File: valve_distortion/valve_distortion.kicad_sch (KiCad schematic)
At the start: 30 parts, among them J1 INPUT, J2 OUTPUT, J3 Barrel_Jack, SW1 SW_DPDT_x2, U1 12AX7, U2 TL074

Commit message: Finish layout
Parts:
- removed D1: ENABLE, Connector_PinHeader_2.54mm:PinHeader_1x02_P2.54mm_Vertical, symbol Device:LED
- removed R5: 100k, Resistor_THT:R_Axial_DIN0207_L6.3mm_D2.5mm_P10.16mm_Horizontal, symbol Device:R
- added C5: 16pF, Capacitor_THT:C_Disc_D3.0mm_W1.6mm_P2.50mm, symbol Device:C_Small
- added D1: LED IND 12V, Connector_PinHeader_2.54mm:PinHeader_1x02_P2.54mm_Vertical, symbol Connector_Generic:Conn_01x02
- added D3: 1N5817, Diode_THT:D_DO-41_SOD81_P10.16mm_Horizontal, symbol Diode:1N5817
- added Q1: 2N3904, Package_TO_SOT_THT:TO-92_Inline, symbol Transistor_BJT:2N3904
- added R11, R13, R7, R8: 100k, Resistor_THT:R_Axial_DIN0207_L6.3mm_D2.5mm_P10.16mm_Horizontal, symbol Device:R
- added R2: 100R, Resistor_THT:R_Axial_DIN0207_L6.3mm_D2.5mm_P10.16mm_Horizontal, symbol Device:R
- D2: value SIGNAL -> NTE30033
- J1, J2: footprint Connector_Molex:Molex_KK-254_AE-6410-02A_1x02_P2.54mm_Vertical -> Connector_PinHeader_2.54mm:PinHeader_1x02_P2.54mm_Vertical
- R12: renamed from R7; value 1k -> 470R
- R6: value 1k -> 100k
- RV4: value R_Potentiometer_Trim -> 200k; footprint Potentiometer_THT:Potentiometer_Bourns_3266Y_Vertical -> valve_distortion:Trimmer
- renumbered C9 to C10, C5 to C6, C6 to C7, C7 to C8, C8 to C9, R9 to R10, R2 to R3, R3 to R5, R8 to R9
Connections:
- net +12V: now also SW1.4 (A), D3.1 (K); no longer J3.1, SW1.5 (B)
- net GND: now also SW1.6 (C), U1.3 (K), D1.2 (Pin_2), Q1.1 (E); no longer D2.1 (K), U1.8 (K)
- net VBIAS: now also U2.10 (+), U2.5 (+), R11.1, R7.2; no longer C8.1, U2.1, U2.12 (+), U2.2 (-)
- net at C3.1, R5.2: now also U1.1 (A); no longer U1.6 (A)
- net at C2.1, R4.1: now also U1.2 (G); no longer U1.7 (G)
- net at C2.2, R3.2: now also U1.6 (A); no longer U1.1 (A)
- net at C1.1, R1.1: now also U1.7 (G); no longer U1.2 (G)
- net at RV1.3: now also R2.2; no longer U1.3 (K)
- net at C3.2, C4.2: now also R6.2; no longer U2.10 (+), U2.5 (+)
- net at U2.6 (-): now also R6.1, C5.2, R7.1, R8.2; no longer RV4.2
- net at R12.1: now also U2.14; no longer U2.7
- net at U2.8, U2.9 (-): no longer C6.1
- net at U2.13 (-): now also RV4.2; no longer U2.14
- new net: R2.1, U1.8 (K)
- new net: C8.1, R11.2, U2.1, U2.2 (-)
- new net: Q1.2 (B), R13.1
- new net: D2.1 (K), Q1.3 (C)
- new net: D3.2 (A), J3.1
- new net BUF_OUT: C5.1, C6.1, R8.1, U2.12 (+), U2.7
- new net ENABLE: D1.1 (Pin_1), R13.2, SW1.5 (B)
- no-connect marks 2 -> 1
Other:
- note added: "ENABLE LED"
- note added: "Inverting Summer Gain = -1"
- note added: "SIGNAL LED"
- note removed: "GAIN"
- note removed: "RC High-pass Fc = ~3.4Hz"
- note removed: "RC High-pass Fc = ~7.2Hz"
- note removed: "TONE"
- note removed: "VOLUME"
- moved on the sheet: C1, C10, C2, C3, C6, C7, C8, C9, D2, J1, J2, J3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

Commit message: Include changes from scehmatic review
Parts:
- removed R11: 100k, Resistor_THT:R_Axial_DIN0207_L6.3mm_D2.5mm_P10.16mm_Horizontal, symbol Device:R
- added R12, R8: 100k, Resistor_THT:R_Axial_DIN0207_L6.3mm_D2.5mm_P10.16mm_Horizontal, symbol Device:R
- renumbered R9 to R10, R10 to R11, R12 to R13, R13 to R14, R7 to R6, R6 to R7, R8 to R9
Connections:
- net VBIAS: now also C8.1, U2.1, U2.2 (-), R12.2, R8.2; no longer U2.10 (+), U2.5 (+)
- new net: R8.1, U2.5 (+)
- new net: R12.1, U2.10 (+)
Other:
- moved on the sheet: C4, C5, C6, C7, C8, D1, J2, R10, R11, R6, R7, R9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

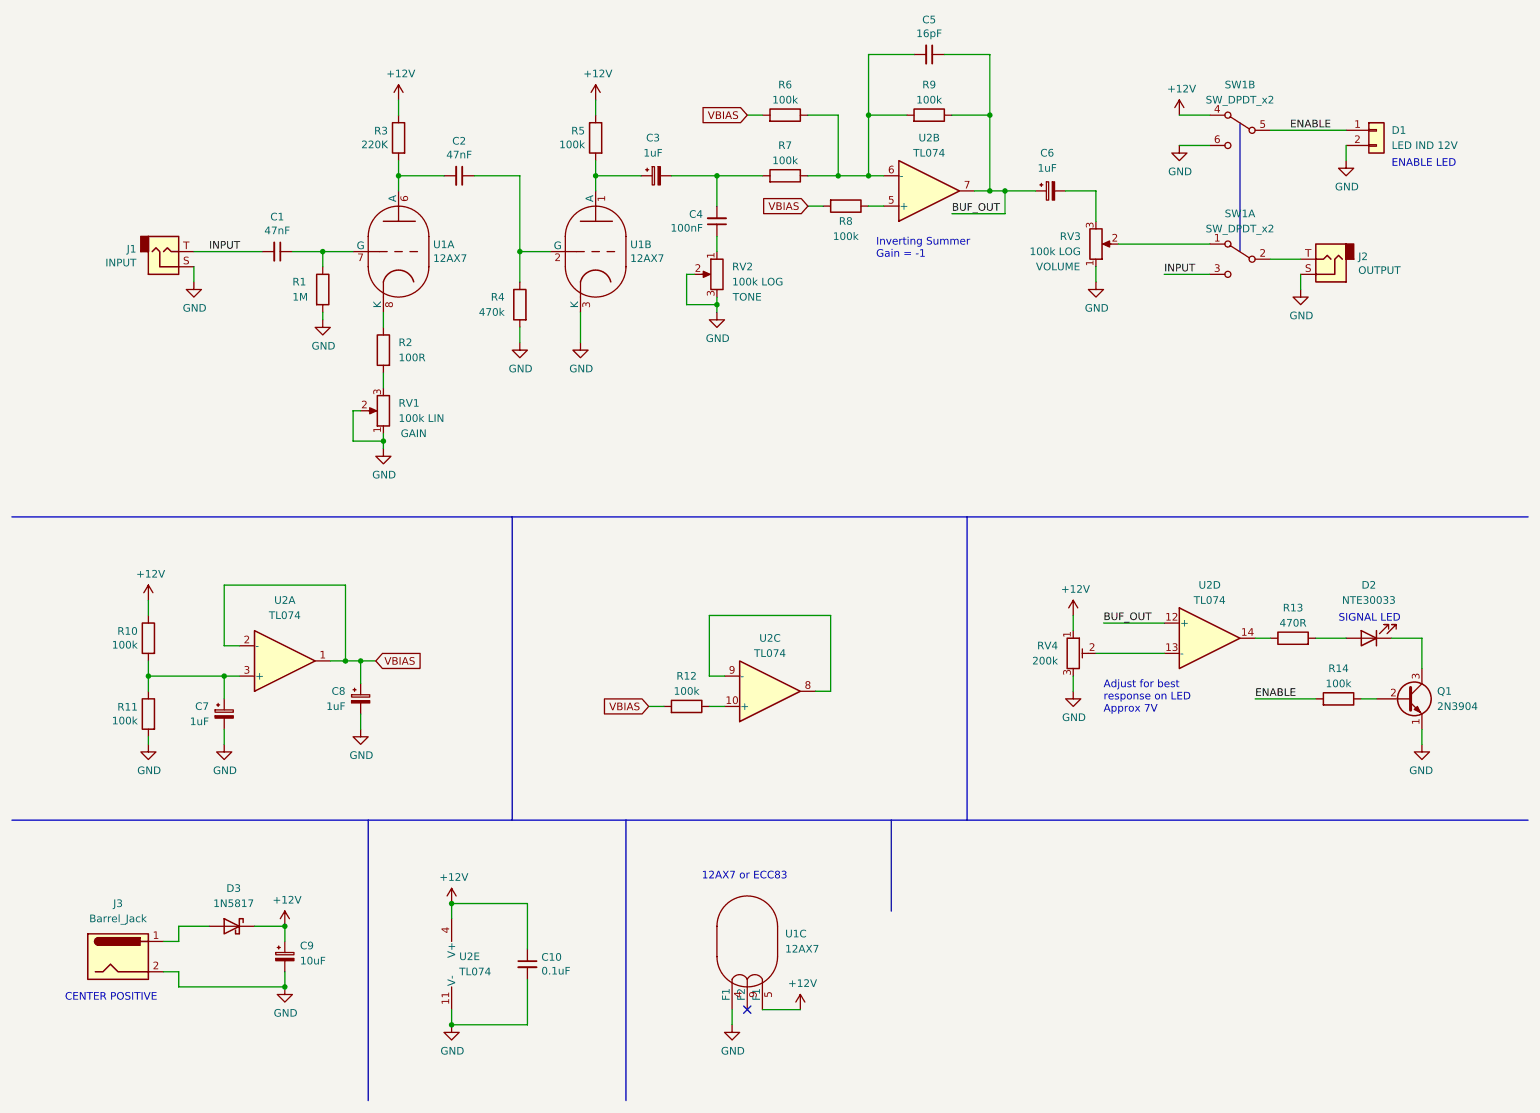
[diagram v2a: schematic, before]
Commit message: Address opamp cap load
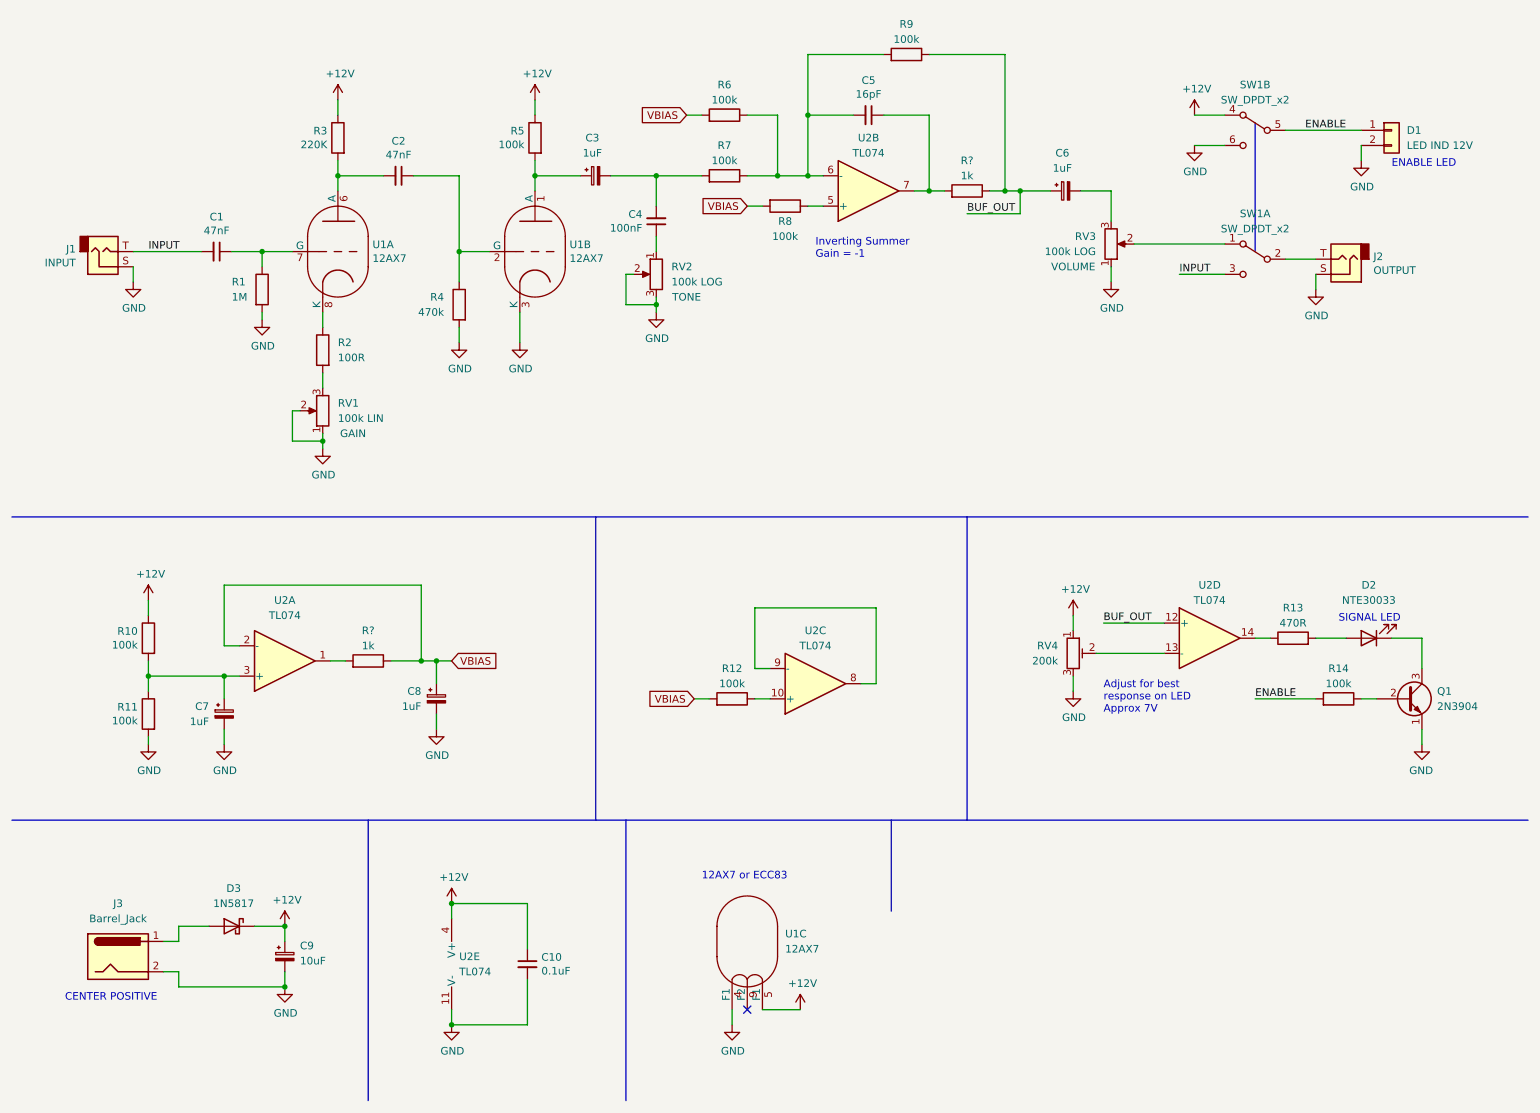
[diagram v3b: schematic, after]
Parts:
- added R? (x2): 1k, Resistor_THT:R_Axial_DIN0207_L6.3mm_D2.5mm_P10.16mm_Horizontal, symbol Device:R
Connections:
- net BUF_OUT: now also R?.1; no longer C5.1, U2.7
- net VBIAS: now also R?.1; no longer U2.1
- new net: R?.2, U2.1
- new net: C5.1, R?.2, U2.7
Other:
- moved on the sheet: C1, C2, C3, C4, C5, C6, C8, D1, J1, J2, R1, R12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
